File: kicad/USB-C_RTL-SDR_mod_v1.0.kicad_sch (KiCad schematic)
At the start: 8 parts, among them J1 USB_C_Receptacle_USB2.0, J2 USB_A

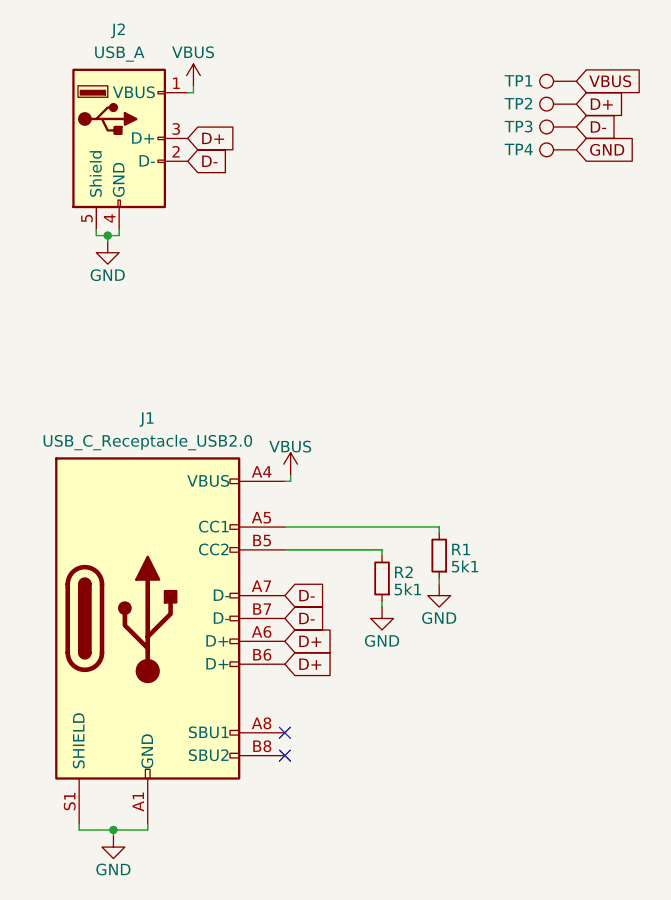
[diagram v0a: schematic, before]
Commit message: Update component properties in schematic: modify BOM inclusion and DNP status for several components, and add LCSC properties for new components.
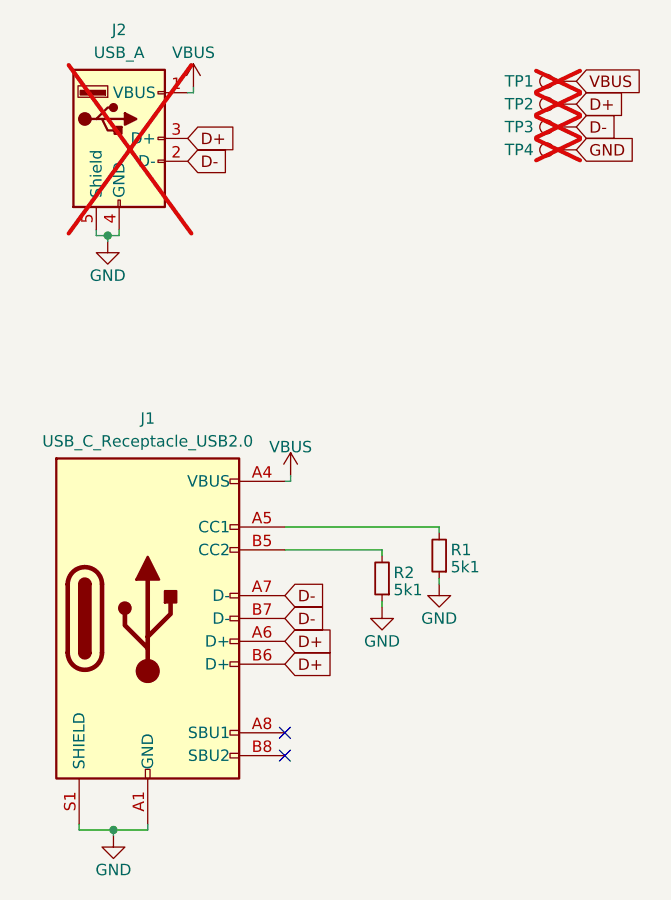
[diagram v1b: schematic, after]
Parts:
- J1: LCSC (none) -> C2988369
- J2, TP1, TP2, TP3, TP4: now not fitted; now left out of the parts list
- R1, R2: LCSC (none) -> C25905
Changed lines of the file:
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@@
+			)
+		)
+		(property "LCSC" "C25905"
+			(at 157.48 114.935 0)
+			(effects
+				(font
+					(size 1.27 1.27)
+				)
+				(hide yes)
 			)
 		)
@@
 		(unit 1)
 		(exclude_from_sim no)
-		(in_bom yes)
+		(in_bom no)
 		(on_board no)
-		(dnp no)
+		(dnp yes)
 		(property "Reference" "TP2"
 			(at 172.72 62.23 90)
@@
 		(unit 1)
 		(exclude_from_sim no)
-		(in_bom yes)
+		(in_bom no)
 		(on_board no)
-		(dnp no)
+		(dnp yes)
 		(property "Reference" "TP4"
 			(at 172.72 67.31 90)
@@
 		(unit 1)
 		(exclude_from_sim no)
-		(in_bom yes)
+		(in_bom no)
 		(on_board no)
-		(dnp no)
+		(dnp yes)
 		(property "Reference" "TP1"
 			(at 172.72 59.69 90)
@@
 			)
 		)
+		(property "LCSC" "C2988369"
+			(at 131.445 119.38 0)
+			(effects
+				(font
+					(size 1.27 1.27)
+				)
+				(hide yes)
+			)
+		)
 		(pin "A1"
 		)
@@
 			)
 		)
+		(property "LCSC" "C25905"
+			(at 163.83 112.395 0)
+			(effects
+				(font
+					(size 1.27 1.27)
+				)
+				(hide yes)
+			)
+		)
 		(pin "1"
 		)
@@
 		(unit 1)
 		(exclude_from_sim no)
-		(in_bom yes)
+		(in_bom no)
 		(on_board yes)
-		(dnp no)
+		(dnp yes)
 		(property "Reference" "J2"
 			(at 128.27 53.975 0)
@@
 			)
 		)
-		(property "Datasheet" " ~"
+		(property "Datasheet" "~"
 			(at 132.08 67.31 0)
 			(effects
@@
 		(unit 1)
 		(exclude_from_sim no)
-		(in_bom yes)
+		(in_bom no)
 		(on_board no)
-		(dnp no)
+		(dnp yes)
 		(property "Reference" "TP3"
 			(at 172.72 64.77 90)
